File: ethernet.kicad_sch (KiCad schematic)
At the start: 43 parts, among them U1 24AA02-OT, U2 W5500, Y1 25MHz

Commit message: fix some lingering issues
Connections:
- net +3V3: now also R11.1
- net ETH_CD: now reaches R11.2
- net ETH_CD: now also C10.1
- net RDN renamed ETH_RDN
- net RDP renamed ETH_RDP
- net TDN renamed ETH_TDN
- net TDP renamed ETH_TDP
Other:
- note removed: "???: is EEPROM still needed?"
- note removed: "???: what are these for?"
- company: (none) -> github.com/westrik
- title: (none) -> NA-01 Time Computer
- moved on the sheet: C10, C2, C4, C5, C6, R11, R3, R6, R7, R8

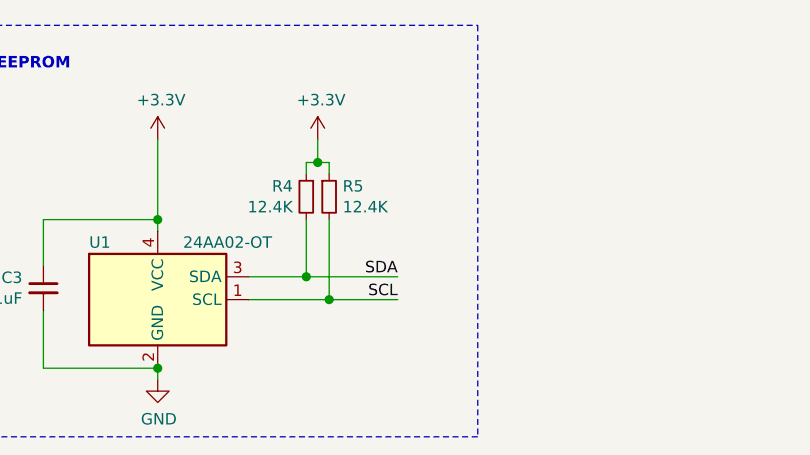
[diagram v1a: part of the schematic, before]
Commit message: hook up mac eeprom to i2c
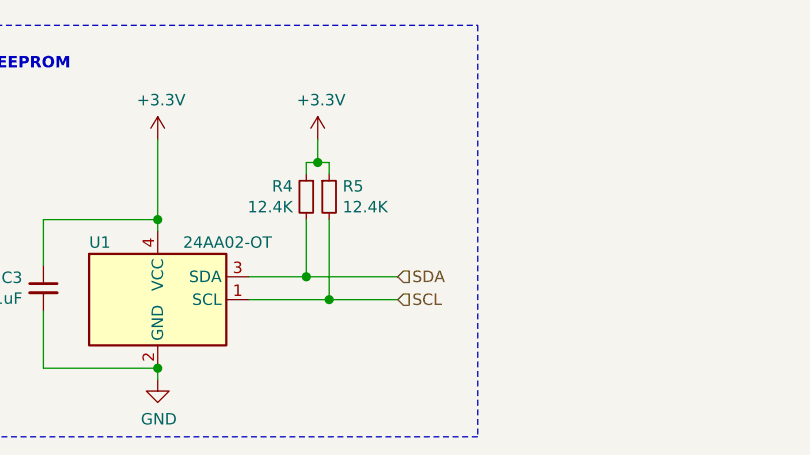
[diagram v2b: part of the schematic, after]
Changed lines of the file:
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@@
     (effects (font (size 1.27 1.27) (thickness 0.254) bold) (justify left bottom))
-  )
-  (label "SDA" (at 68.58 182.88 180)
-    (effects (font (size 1.27 1.27)) (justify right bottom))
-  )
-  (label "SCL" (at 68.58 185.42 180)
-    (effects (font (size 1.27 1.27)) (justify right bottom))
   )
   (label "TXP" (at 113.03 45.72 180)
@@
     (effects (font (size 1.27 1.27)) (justify right))
   )
+  (hierarchical_label "SDA" (shape input) (at 68.58 182.88 0)
+    (effects (font (size 1.27 1.27)) (justify left))
+  )
+  (hierarchical_label "SCL" (shape input) (at 68.58 185.42 0)
+    (effects (font (size 1.27 1.27)) (justify left))
+  )
   (hierarchical_label "ETHLINKLED" (shape output) (at 252.73 20.32 0)

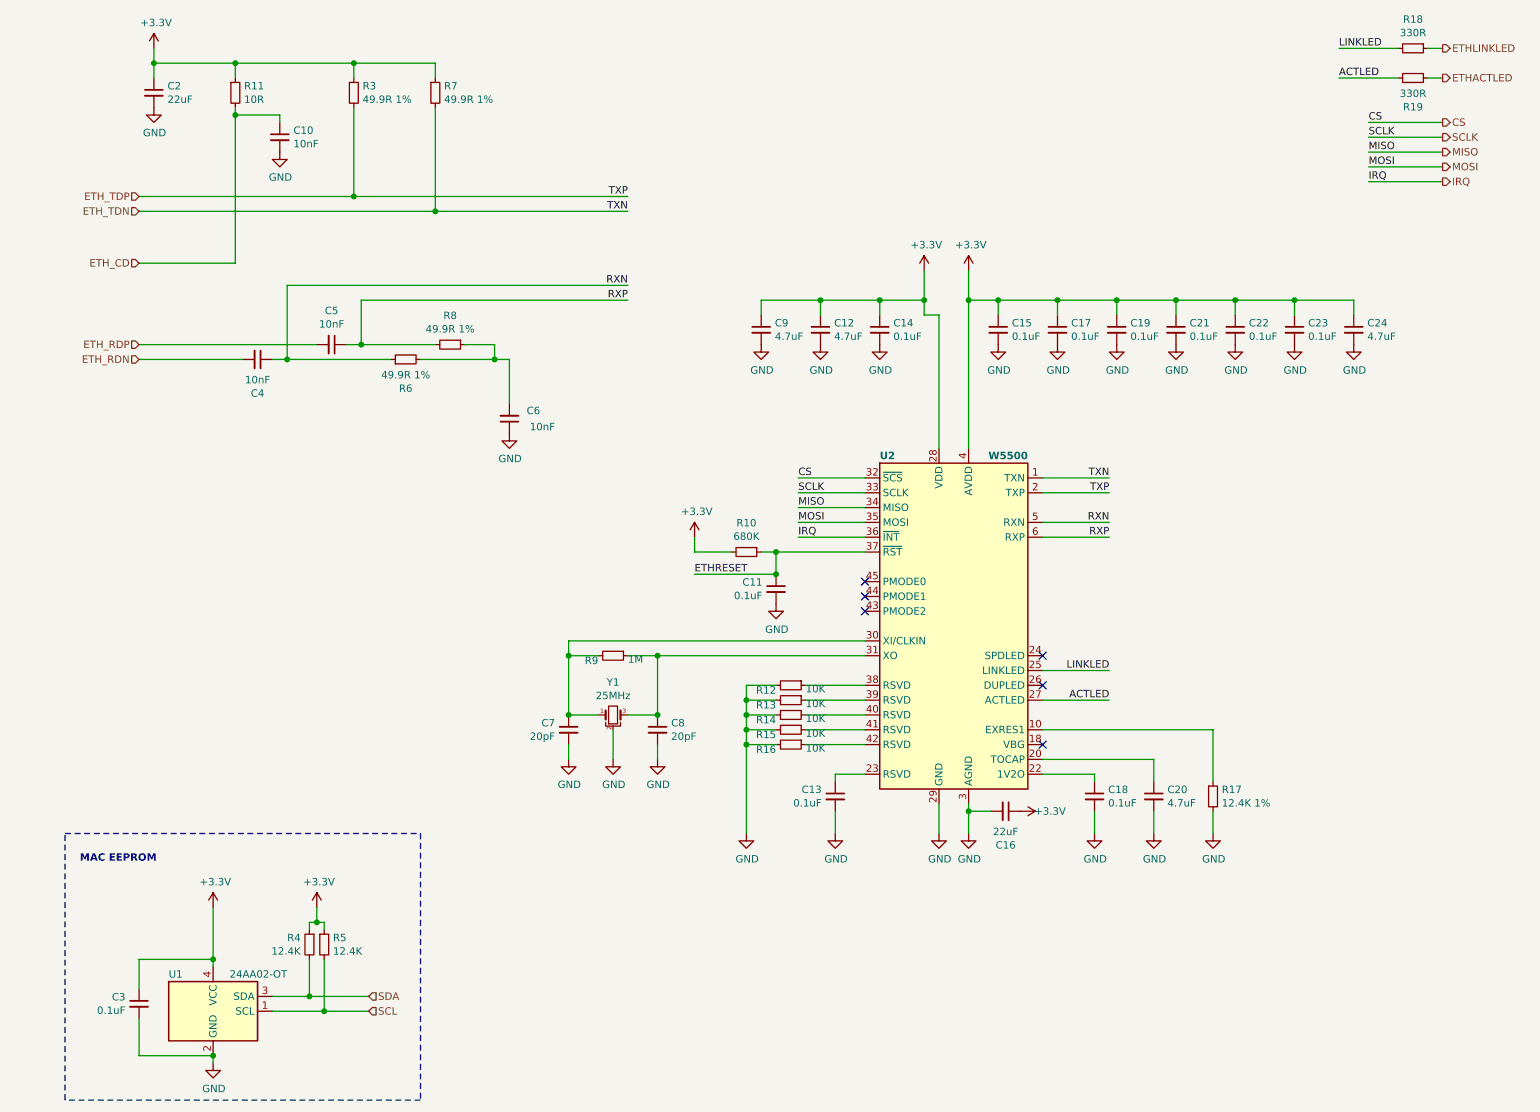
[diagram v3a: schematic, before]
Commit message: rough component placement
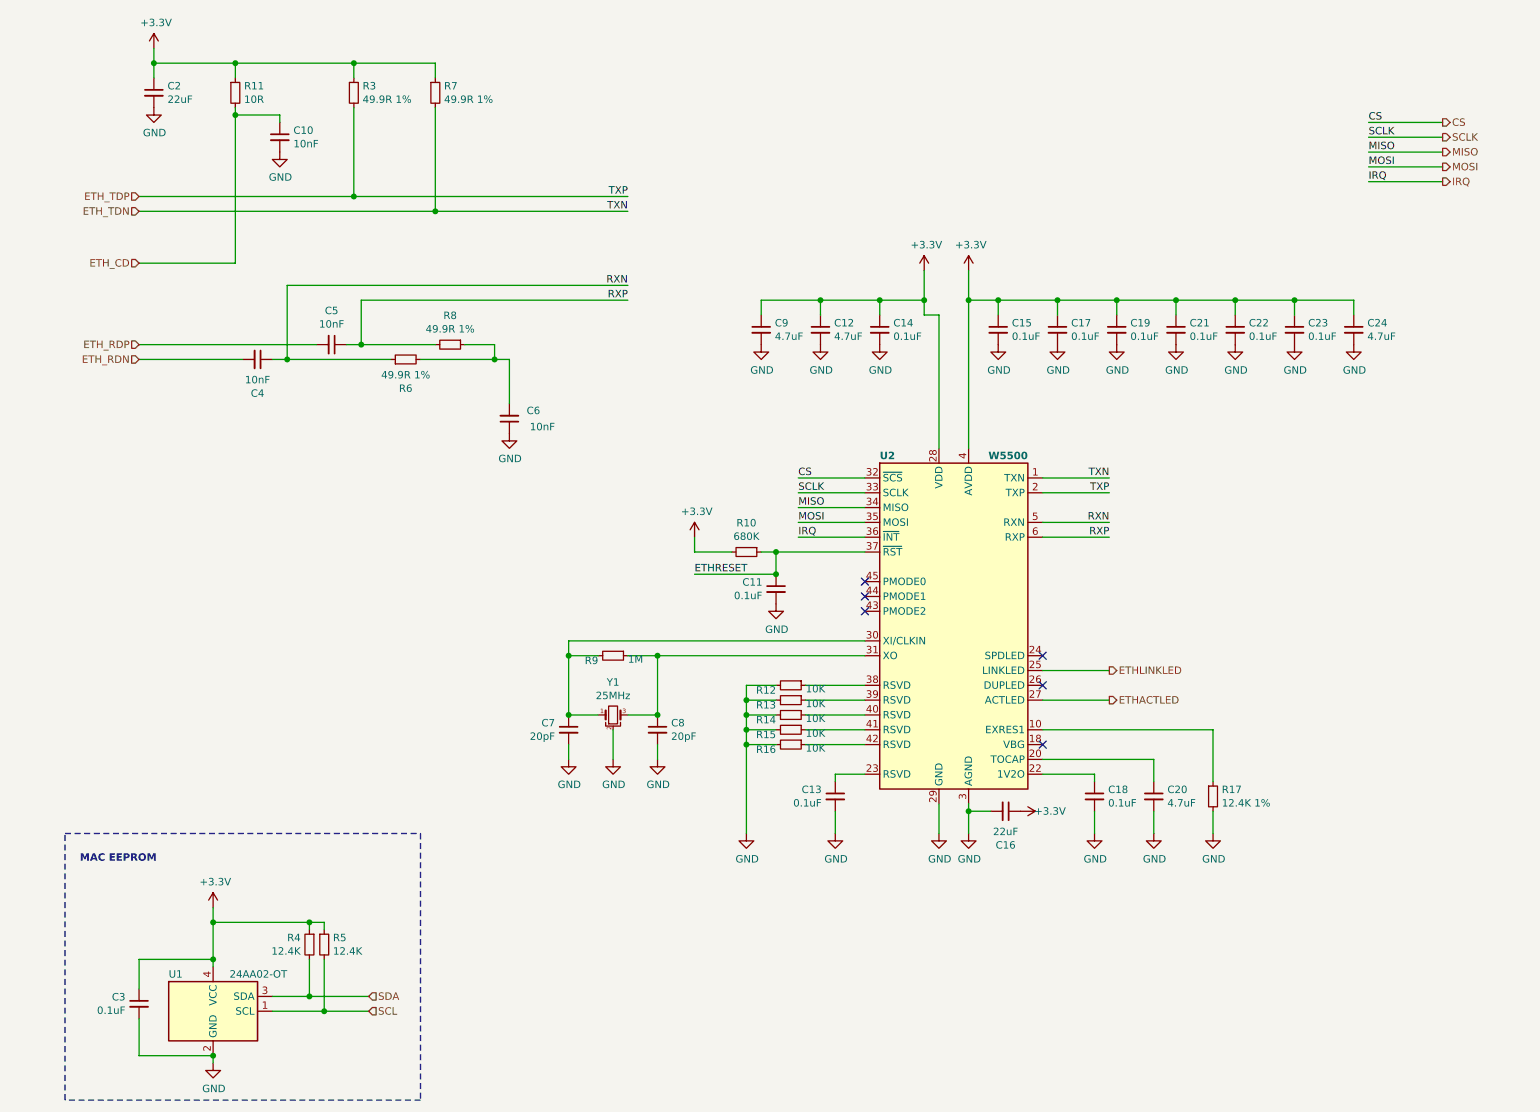
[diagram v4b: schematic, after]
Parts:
- removed R18, R19: 330R, Resistor_SMD:R_0402_1005Metric, symbol PoE-NTP-Clock-rescue:R_Small-Device
- C10, C11, C12, C13, C14, C15, C17, C18, C19, C20, C21, C22, C23, C24, C3, C4, C5, C6, C7, C8, C9: symbol PoE-NTP-Clock-rescue:C_Small-Device -> Device:C_Small
- C16, C2: footprint Capacitor_SMD:C_0402_1005Metric -> Capacitor_SMD:C_0805_2012Metric; symbol PoE-NTP-Clock-rescue:C_Small-Device -> Device:C_Small
- R10: footprint Resistor_SMD:R_0402_1005Metric -> Resistor_SMD:R_0603_1608Metric; symbol PoE-NTP-Clock-rescue:R_Small-Device -> Device:R_Small
- R11, R12, R13, R14, R15, R16, R17, R3, R4, R5, R6, R7, R8, R9: symbol PoE-NTP-Clock-rescue:R_Small-Device -> Device:R_Small
- U1: symbol PoE-NTP-Clock-rescue:24AA02-OT-Memory_EEPROM -> Memory_EEPROM:24AA02-OT
- U2: symbol PoE-NTP-Clock-rescue:W5500-Interface_Ethernet -> Interface_Ethernet:W5500
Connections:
- net ACTLED is gone; now on net ETHACTLED: U2.27 (ACTLED)
- net LINKLED is gone; now on net ETHLINKLED: U2.25 (LINKLED)

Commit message: add some part numbers to schematic
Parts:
- C10, C4, C5, C6: LCSC Part Number (none) -> C15195
- C11, C13, C14, C15, C17, C18, C19, C21, C22, C23, C3: LCSC Part Number (none) -> C1525
- C12, C20, C24, C9: LCSC Part Number (none) -> C23733
- C16, C2: LCSC Part Number (none) -> C59461
- C7, C8: LCSC Part Number (none) -> C1554
- R3, R6, R7, R8: LCSC Part Number (none) -> C25120
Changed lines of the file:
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@@
+      (effects (font (size 1.27 1.27)) hide)
+    )
+    (property "LCSC Part Number" "C25120" (id 4) (at 66.04 27.94 0)
       (effects (font (size 1.27 1.27)) hide)
     )
@@
       (effects (font (size 1.27 1.27)) hide)
     )
+    (property "LCSC Part Number" "C25120" (id 4) (at 74.93 73.66 0)
+      (effects (font (size 1.27 1.27)) hide)
+    )
   )
   (symbol (lib_id "Device:R_Small") (at 80.01 27.94 0) (unit 1)
@@
     )
     (property "Datasheet" "~" (id 3) (at 80.01 27.94 0)
+      (effects (font (size 1.27 1.27)) hide)
+    )
+    (property "LCSC Part Number" "C25120" (id 4) (at 80.01 27.94 0)
       (effects (font (size 1.27 1.27)) hide)
     )
@@
       (effects (font (size 1.27 1.27)) hide)
     )
+    (property "LCSC Part Number" "C25120" (id 4) (at 82.55 71.12 0)
+      (effects (font (size 1.27 1.27)) hide)
+    )
   )
   (symbol (lib_id "Device:R_Small") (at 110.49 124.46 270) (unit 1)
@@
       (effects (font (size 1.27 1.27)) hide)
     )
+    (property "LCSC Part Number" "C1525" (id 4) (at 29.21 184.15 0)
+      (effects (font (size 1.27 1.27)) hide)
+    )
   )
   (symbol (lib_id "Device:C_Small") (at 31.75 27.94 0) (unit 1)
@@
     )
     (property "Datasheet" "~" (id 3) (at 31.75 27.94 0)
+      (effects (font (size 1.27 1.27)) hide)
+    )
+    (property "LCSC Part Number" "C59461" (id 4) (at 31.75 27.94 0)
       (effects (font (size 1.27 1.27)) hide)
     )
@@
       (effects (font (size 1.27 1.27)) hide)
     )
+    (property "LCSC Part Number" "C15195" (id 4) (at 49.53 73.66 0)
+      (effects (font (size 1.27 1.27)) hide)
+    )
   )
   (symbol (lib_id "Device:C_Small") (at 53.34 35.56 0) (unit 1)
@@
     )
     (property "Datasheet" "~" (id 3) (at 53.34 35.56 0)
+      (effects (font (size 1.27 1.27)) hide)
+    )
+    (property "LCSC Part Number" "C15195" (id 4) (at 53.34 35.56 0)
       (effects (font (size 1.27 1.27)) hide)
     )
@@
       (effects (font (size 1.27 1.27)) hide)
     )
+    (property "LCSC Part Number" "C15195" (id 4) (at 62.23 71.12 0)
+      (effects (font (size 1.27 1.27)) hide)
+    )
   )
   (symbol (lib_id "Device:C_Small") (at 92.71 83.82 180) (unit 1)
@@
       (effects (font (size 1.27 1.27)) hide)
     )
+    (property "LCSC Part Number" "C15195" (id 4) (at 92.71 83.82 0)
+      (effects (font (size 1.27 1.27)) hide)
+    )
   )
   (symbol (lib_id "Device:C_Small") (at 102.87 137.16 0) (mirror y) (unit 1)
@@
       (effects (font (size 1.27 1.27)) hide)
     )
+    (property "LCSC Part Number" "C1554" (id 4) (at 102.87 137.16 0)
+      (effects (font (size 1.27 1.27)) hide)
+    )
   )
   (symbol (lib_id "Device:C_Small") (at 118.11 137.16 0) (unit 1)
@@
       (effects (font (size 1.27 1.27)) hide)
     )
+    (property "LCSC Part Number" "C1554" (id 4) (at 118.11 137.16 0)
+      (effects (font (size 1.27 1.27)) hide)
+    )
   )
   (symbol (lib_id "Device:C_Small") (at 135.89 68.58 0) (unit 1)
@@
       (effects (font (size 1.27 1.27)) hide)
     )
+    (property "LCSC Part Number" "C23733" (id 4) (at 135.89 68.58 0)
+      (effects (font (size 1.27 1.27)) hide)
+    )
   )
   (symbol (lib_id "Device:C_Small") (at 138.43 113.03 0) (mirror y) (unit 1)
@@
       (effects (font (size 1.27 1.27)) hide)
     )
+    (property "LCSC Part Number" "C1525" (id 4) (at 138.43 113.03 0)
+      (effects (font (size 1.27 1.27)) hide)
+    )
   )
   (symbol (lib_id "Device:C_Small") (at 146.05 68.58 0) (unit 1)
@@
       (effects (font (size 1.27 1.27)) hide)
     )
+    (property "LCSC Part Number" "C23733" (id 4) (at 146.05 68.58 0)
+      (effects (font (size 1.27 1.27)) hide)
+    )
   )
   (symbol (lib_id "Device:C_Small") (at 148.59 148.59 0) (mirror y) (unit 1)
@@
       (effects (font (size 1.27 1.27)) hide)
     )
+    (property "LCSC Part Number" "C1525" (id 4) (at 148.59 148.59 0)
+      (effects (font (size 1.27 1.27)) hide)
+    )
   )
   (symbol (lib_id "Device:C_Small") (at 156.21 68.58 0) (unit 1)
@@
       (effects (font (size 1.27 1.27)) hide)
     )
+    (property "LCSC Part Number" "C1525" (id 4) (at 156.21 68.58 0)
+      (effects (font (size 1.27 1.27)) hide)
+    )
   )
   (symbol (lib_id "Device:C_Small") (at 176.53 68.58 0) (unit 1)
@@
     )
     (property "Datasheet" "~" (id 3) (at 176.53 68.58 0)
+      (effects (font (size 1.27 1.27)) hide)
+    )
+    (property "LCSC Part Number" "C1525" (id 4) (at 176.53 68.58 0)
       (effects (font (size 1.27 1.27)) hide)
     )
@@
       (effects (font (size 1.27 1.27)) hide)
     )
+    (property "LCSC Part Number" "C59461" (id 4) (at 177.8 151.13 0)
+      (effects (font (size 1.27 1.27)) hide)
+    )
   )
   (symbol (lib_id "Device:C_Small") (at 186.69 68.58 0) (unit 1)
@@
       (effects (font (size 1.27 1.27)) hide)
     )
+    (property "LCSC Part Number" "C1525" (id 4) (at 186.69 68.58 0)
+      (effects (font (size 1.27 1.27)) hide)
+    )
   )
   (symbol (lib_id "Device:C_Small") (at 193.04 148.59 0) (unit 1)
@@
       (effects (font (size 1.27 1.27)) hide)
     )
+    (property "LCSC Part Number" "C1525" (id 4) (at 193.04 148.59 0)
+      (effects (font (size 1.27 1.27)) hide)
+    )
   )
   (symbol (lib_id "Device:C_Small") (at 196.85 68.58 0) (unit 1)
@@
       (effects (font (size 1.27 1.27)) hide)
     )
+    (property "LCSC Part Number" "C1525" (id 4) (at 196.85 68.58 0)
+      (effects (font (size 1.27 1.27)) hide)
+    )
   )
   (symbol (lib_id "Device:C_Small") (at 203.2 148.59 0) (unit 1)
@@
       (effects (font (size 1.27 1.27)) hide)
     )
+    (property "LCSC Part Number" "C23733" (id 4) (at 203.2 148.59 0)
+      (effects (font (size 1.27 1.27)) hide)
+    )
   )
   (symbol (lib_id "Device:C_Small") (at 207.01 68.58 0) (unit 1)
@@
       (effects (font (size 1.27 1.27)) hide)
     )
+    (property "LCSC Part Number" "C1525" (id 4) (at 207.01 68.58 0)
+      (effects (font (size 1.27 1.27)) hide)
+    )
   )
   (symbol (lib_id "Device:C_Small") (at 217.17 68.58 0) (unit 1)
@@
       (effects (font (size 1.27 1.27)) hide)
     )
+    (property "LCSC Part Number" "C1525" (id 4) (at 217.17 68.58 0)
+      (effects (font (size 1.27 1.27)) hide)
+    )
   )
   (symbol (lib_id "Device:C_Small") (at 227.33 68.58 0) (unit 1)
@@
       (effects (font (size 1.27 1.27)) hide)
     )
+    (property "LCSC Part Number" "C1525" (id 4) (at 227.33 68.58 0)
+      (effects (font (size 1.27 1.27)) hide)
+    )
   )
   (symbol (lib_id "Device:C_Small") (at 237.49 68.58 0) (unit 1)
@@
       (effects (font (size 1.27 1.27)) hide)
     )
+    (property "LCSC Part Number" "C23733" (id 4) (at 237.49 68.58 0)
+      (effects (font (size 1.27 1.27)) hide)
+    )
